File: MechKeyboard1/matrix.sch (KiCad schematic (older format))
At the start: 134 parts, among them SW10 SW_Push, SW11 SW_Push, SW12 SW_Push, SW13 SW_Push, SW14 SW_Push, SW15 SW_Push, SW16 SW_Push, SW17 SW_Push, SW18 SW_Push, SW19 SW_Push, SW2 SW_Push, SW20 SW_Push, SW21 SW_Push, SW22 SW_Push, SW23 SW_Push, SW24 SW_Push, SW25 SW_Push, SW26 SW_Push, SW27 SW_Push, SW28 SW_Push, SW29 SW_Push, SW3 SW_Push, SW30 SW_Push, SW31 SW_Push, SW32 SW_Push, SW33 SW_Push, SW34 SW_Push, SW35 SW_Push, SW36 SW_Push, SW37 SW_Push, SW38 SW_Push, SW39 SW_Push, SW4 SW_Push, SW40 SW_Push, SW41 SW_Push, SW42 SW_Push, SW43 SW_Push, SW44 SW_Push, SW45 SW_Push, SW46 SW_Push, SW47 SW_Push, SW48 SW_Push, SW49 SW_Push, SW5 SW_Push, SW50 SW_Push, SW51 SW_Push, SW52 SW_Push, SW53 SW_Push, SW54 SW_Push, SW55 SW_Push, SW56 SW_Push, SW57 SW_Push, SW58 SW_Push, SW59 SW_Push, SW6 SW_Push, SW60 SW_Push, SW61 SW_Push, SW62 SW_Push, SW63 SW_Push, SW64 SW_Push, SW65 SW_Push, SW66 SW_Push, SW67 SW_Push, SW68 SW_Push, SW7 SW_Push, SW8 SW_Push, SW9 SW_Push

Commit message: Redo Naming Matrix
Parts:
- removed SW10, SW11, SW12, SW13, SW14, SW15, SW16, SW17, SW18, SW19, SW20, SW21, SW22, SW23, SW24, SW25, SW26, SW27, SW28, SW29, SW3, SW30, SW31, SW32, SW33, SW34, SW35, SW36, SW37, SW38, SW39, SW4, SW40, SW41, SW42, SW43, SW44, SW45, SW46, SW47, SW48, SW49, SW5, SW50, SW51, SW52, SW53, SW54, SW55, SW56, SW57, SW58, SW59, SW6, SW60, SW61, SW62, SW63, SW64, SW65, SW66, SW67, SW68, SW7, SW8, SW9: SW_Push, symbol Switch:SW_Push
- added K10: #9, symbol Switch:SW_Push
- added K11: #0, symbol Switch:SW_Push
- added K12: -_, symbol Switch:SW_Push
- added K13: =+, symbol Switch:SW_Push
- added K14: BSPC, symbol Switch:SW_Push
- added K15: PGUP, symbol Switch:SW_Push
- added K16: TAB, symbol Switch:SW_Push
- added K17: Q, symbol Switch:SW_Push
- added K18: W, symbol Switch:SW_Push
- added K19: E, symbol Switch:SW_Push
- added K2: #1, symbol Switch:SW_Push
- added K20: R, symbol Switch:SW_Push
- added K21: T, symbol Switch:SW_Push
- added K22: Y, symbol Switch:SW_Push
- added K23: U, symbol Switch:SW_Push
- added K24: I, symbol Switch:SW_Push
- added K25: O, symbol Switch:SW_Push
- added K26: P, symbol Switch:SW_Push
- added K27: {[, symbol Switch:SW_Push
- added K28: }], symbol Switch:SW_Push
- added K29: \\|, symbol Switch:SW_Push
- added K3: #2, symbol Switch:SW_Push
- added K30: PGDW, symbol Switch:SW_Push
- added K31: CAPS, symbol Switch:SW_Push
- added K32: A, symbol Switch:SW_Push
- added K33: S, symbol Switch:SW_Push
- added K34: D, symbol Switch:SW_Push
- added K35: F, symbol Switch:SW_Push
- added K36: G, symbol Switch:SW_Push
- added K37: H, symbol Switch:SW_Push
- added K38: J, symbol Switch:SW_Push
- added K39: K, symbol Switch:SW_Push
- added K4: #3, symbol Switch:SW_Push
- added K40: L, symbol Switch:SW_Push
- added K41: :;, symbol Switch:SW_Push
- added K42: \"', symbol Switch:SW_Push
- added K43: ENTER, symbol Switch:SW_Push
- added K44: INS, symbol Switch:SW_Push
- added K45: LSHIFT, symbol Switch:SW_Push
- added K46: Z, symbol Switch:SW_Push
- added K47: X, symbol Switch:SW_Push
- added K48: C, symbol Switch:SW_Push
- added K49: V, symbol Switch:SW_Push
- added K5: #4, symbol Switch:SW_Push
- added K50: B, symbol Switch:SW_Push
- added K51: N, symbol Switch:SW_Push
- added K52: M, symbol Switch:SW_Push
- added K53: <,, symbol Switch:SW_Push
- added K54: >., symbol Switch:SW_Push
- added K55: ?/, symbol Switch:SW_Push
- added K56: RSHIFT, symbol Switch:SW_Push
- added K57: UP, symbol Switch:SW_Push
- added K58: DEL, symbol Switch:SW_Push
- added K59: LCTRL, symbol Switch:SW_Push
- added K6: #5, symbol Switch:SW_Push
- added K60: LALT, symbol Switch:SW_Push
- added K61: CMD, symbol Switch:SW_Push
- added K62: SPACE, symbol Switch:SW_Push
- added K63: RALT, symbol Switch:SW_Push
- added K64: FN, symbol Switch:SW_Push
- added K65: LEFT, symbol Switch:SW_Push
- added K66: DOWN, symbol Switch:SW_Push
- added K67: RIGHT, symbol Switch:SW_Push
- added K7: #6, symbol Switch:SW_Push
- added K8: #7, symbol Switch:SW_Push
- added K9: #8, symbol Switch:SW_Push
- K1: renamed from SW2; value SW_Push -> ESC
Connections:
- wire segments 233 -> 301

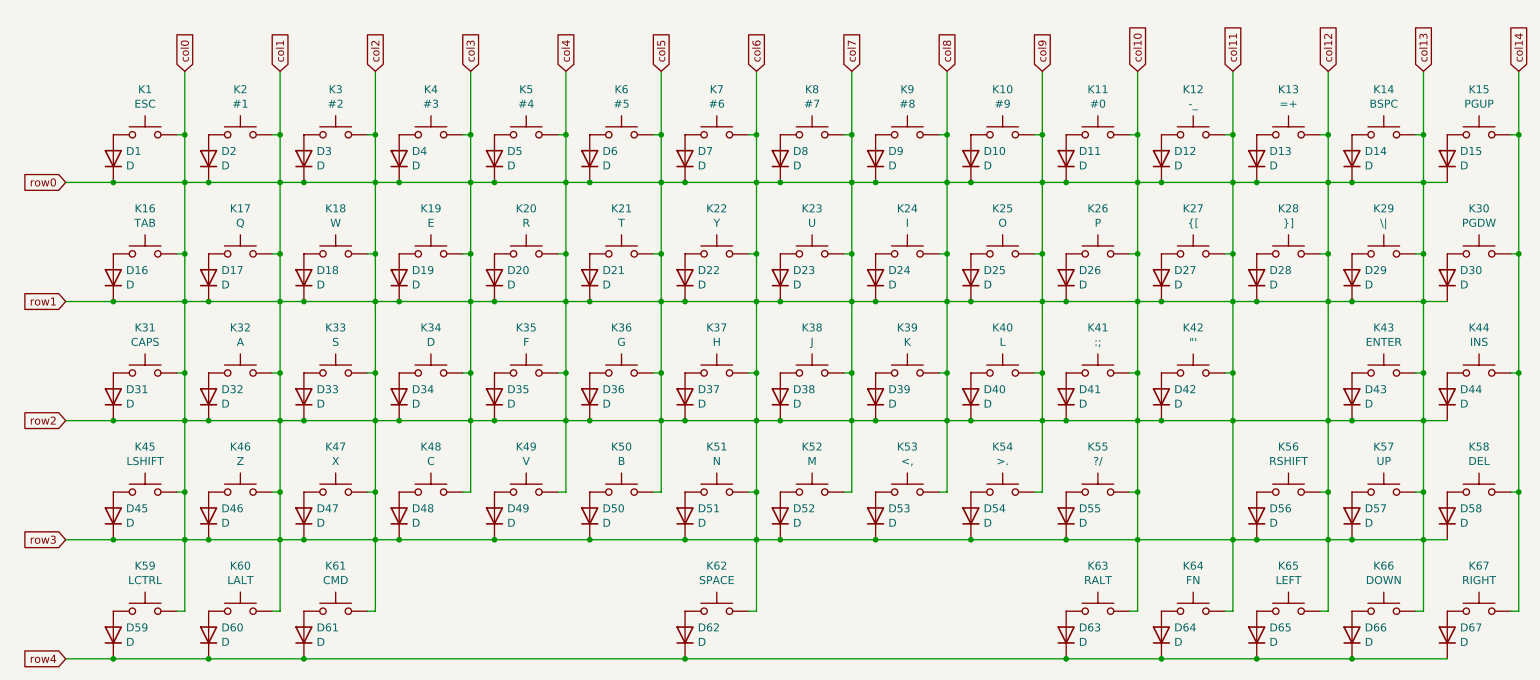
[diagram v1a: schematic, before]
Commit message: Learned Matrix, Annotate, Footprints, & Render Components
*Removed Matrix (caused errors)
*Created Custom Symbols
*Assigned Keys & Layouts
*Rendered Footprints
*Learned Cutting Edges for PCB
*3D Rendered PCB
*Placed ICs to prepare Routing
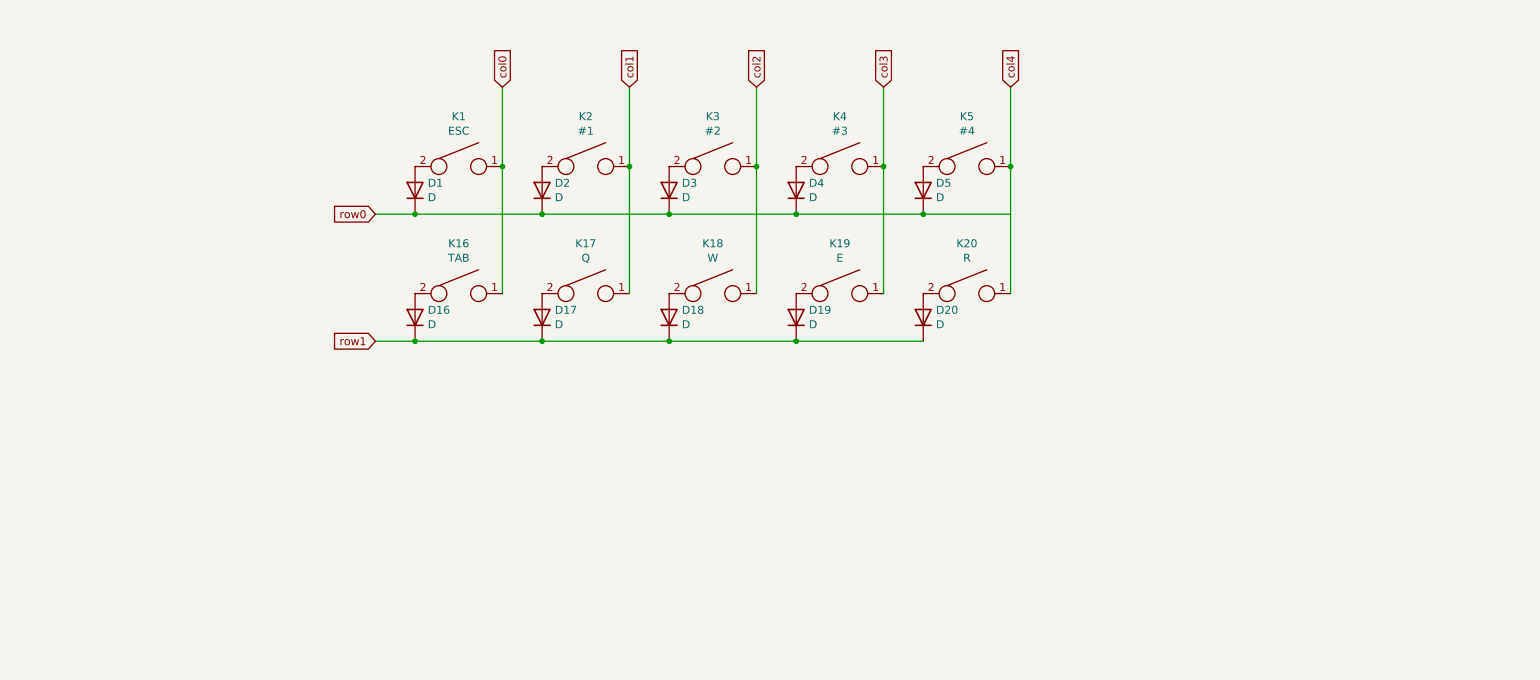
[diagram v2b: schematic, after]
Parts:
- removed D10, D11, D12, D13, D14, D15, D21, D22, D23, D24, D25, D26, D27, D28, D29, D30, D31, D32, D33, D34, D35, D36, D37, D38, D39, D40, D41, D42, D43, D44, D45, D46, D47, D48, D49, D50, D51, D52, D53, D54, D55, D56, D57, D58, D59, D6, D60, D61, D62, D63, D64, D65, D66, D67, D7, D8, D9: D, symbol Device:D
- removed K1: ESC, symbol Switch:SW_Push
- removed K10: #9, symbol Switch:SW_Push
- removed K11: #0, symbol Switch:SW_Push
- removed K12: -_, symbol Switch:SW_Push
- removed K13: =+, symbol Switch:SW_Push
- removed K14: BSPC, symbol Switch:SW_Push
- removed K15: PGUP, symbol Switch:SW_Push
- removed K16: TAB, symbol Switch:SW_Push
- removed K17: Q, symbol Switch:SW_Push
- removed K18: W, symbol Switch:SW_Push
- removed K19: E, symbol Switch:SW_Push
- removed K2: #1, symbol Switch:SW_Push
- removed K20: R, symbol Switch:SW_Push
- removed K21: T, symbol Switch:SW_Push
- removed K22: Y, symbol Switch:SW_Push
- removed K23: U, symbol Switch:SW_Push
- removed K24: I, symbol Switch:SW_Push
- removed K25: O, symbol Switch:SW_Push
- removed K26: P, symbol Switch:SW_Push
- removed K27: {[, symbol Switch:SW_Push
- removed K28: }], symbol Switch:SW_Push
- removed K29: \\|, symbol Switch:SW_Push
- removed K3: #2, symbol Switch:SW_Push
- removed K30: PGDW, symbol Switch:SW_Push
- removed K31: CAPS, symbol Switch:SW_Push
- removed K32: A, symbol Switch:SW_Push
- removed K33: S, symbol Switch:SW_Push
- removed K34: D, symbol Switch:SW_Push
- removed K35: F, symbol Switch:SW_Push
- removed K36: G, symbol Switch:SW_Push
- removed K37: H, symbol Switch:SW_Push
- removed K38: J, symbol Switch:SW_Push
- removed K39: K, symbol Switch:SW_Push
- removed K4: #3, symbol Switch:SW_Push
- removed K40: L, symbol Switch:SW_Push
- removed K41: :;, symbol Switch:SW_Push
- removed K42: \"', symbol Switch:SW_Push
- removed K43: ENTER, symbol Switch:SW_Push
- removed K44: INS, symbol Switch:SW_Push
- removed K45: LSHIFT, symbol Switch:SW_Push
- removed K46: Z, symbol Switch:SW_Push
- removed K47: X, symbol Switch:SW_Push
- removed K48: C, symbol Switch:SW_Push
- removed K49: V, symbol Switch:SW_Push
- removed K5: #4, symbol Switch:SW_Push
- removed K50: B, symbol Switch:SW_Push
- removed K51: N, symbol Switch:SW_Push
- removed K52: M, symbol Switch:SW_Push
- removed K53: <,, symbol Switch:SW_Push
- removed K54: >., symbol Switch:SW_Push
- removed K55: ?/, symbol Switch:SW_Push
- removed K56: RSHIFT, symbol Switch:SW_Push
- removed K57: UP, symbol Switch:SW_Push
- removed K58: DEL, symbol Switch:SW_Push
- removed K59: LCTRL, symbol Switch:SW_Push
- removed K6: #5, symbol Switch:SW_Push
- removed K60: LALT, symbol Switch:SW_Push
- removed K61: CMD, symbol Switch:SW_Push
- removed K62: SPACE, symbol Switch:SW_Push
- removed K63: RALT, symbol Switch:SW_Push
- removed K64: FN, symbol Switch:SW_Push
- removed K65: LEFT, symbol Switch:SW_Push
- removed K66: DOWN, symbol Switch:SW_Push
- removed K67: RIGHT, symbol Switch:SW_Push
- removed K7: #6, symbol Switch:SW_Push
- removed K8: #7, symbol Switch:SW_Push
- removed K9: #8, symbol Switch:SW_Push
- added K1: ESC, Alps_Only:ALPS-1U, symbol Switch:SW_Push2
- added K16: TAB, Alps_Only:ALPS-1.5U, symbol Switch:SW_Push2
- added K17: Q, Alps_Only:ALPS-1U, symbol Switch:SW_Push2
- added K18: W, Alps_Only:ALPS-1U, symbol Switch:SW_Push2
- added K19: E, Alps_Only:ALPS-1U, symbol Switch:SW_Push2
- added K2: #1, Alps_Only:ALPS-1U, symbol Switch:SW_Push2
- added K20: R, Alps_Only:ALPS-1U, symbol Switch:SW_Push2
- added K3: #2, Alps_Only:ALPS-1U, symbol Switch:SW_Push2
- added K4: #3, Alps_Only:ALPS-1U, symbol Switch:SW_Push2
- added K5: #4, Alps_Only:ALPS-1U, symbol Switch:SW_Push2
- D1, D16, D17, D18, D19, D2, D20, D3, D4, D5: footprint (none) -> Diode_SMD:D_0805_2012Metric_Pad1.15x1.40mm_HandSolder
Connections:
- net col0: now also K1.1, K16.1, K17.1, K18.1, K19.1, K2.1, K20.1, K3.1, K4.1, K5.1; no longer D16.1 (K), D17.1 (K), D18.1 (K), D19.1 (K), D20.1 (K)
- net at D2.2 (A): now also K2.2
- net at D3.2 (A): now also K3.2
- net at D4.2 (A): now also K4.2
- net at D5.2 (A): now also K5.2
- net at D1.2 (A): now also K1.2
- net at D16.2 (A): now also K16.2
- net at D17.2 (A): now also K17.2
- net at D18.2 (A): now also K18.2
- net at D19.2 (A): now also K19.2
- net at D20.2 (A): now also K20.2
- new net row1: D16.1 (K), D17.1 (K), D18.1 (K), D19.1 (K), D20.1 (K)
